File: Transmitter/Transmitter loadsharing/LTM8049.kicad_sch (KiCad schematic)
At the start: 9 parts, among them U12 LTM8049IY-PBF

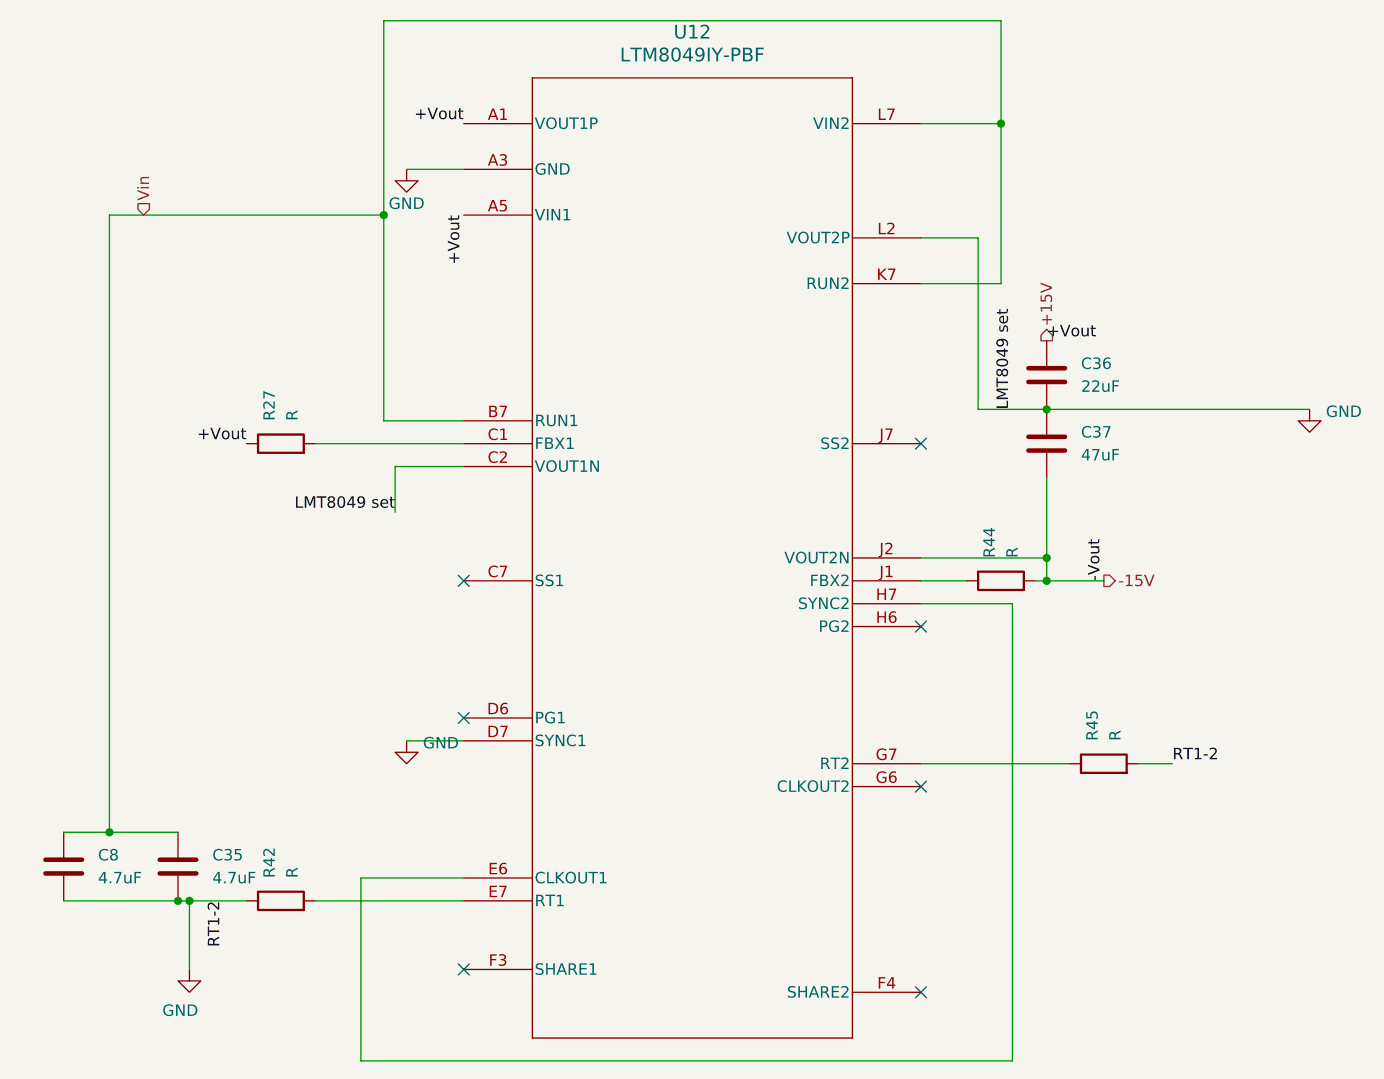
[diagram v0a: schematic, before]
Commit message: routed swithcing regulator
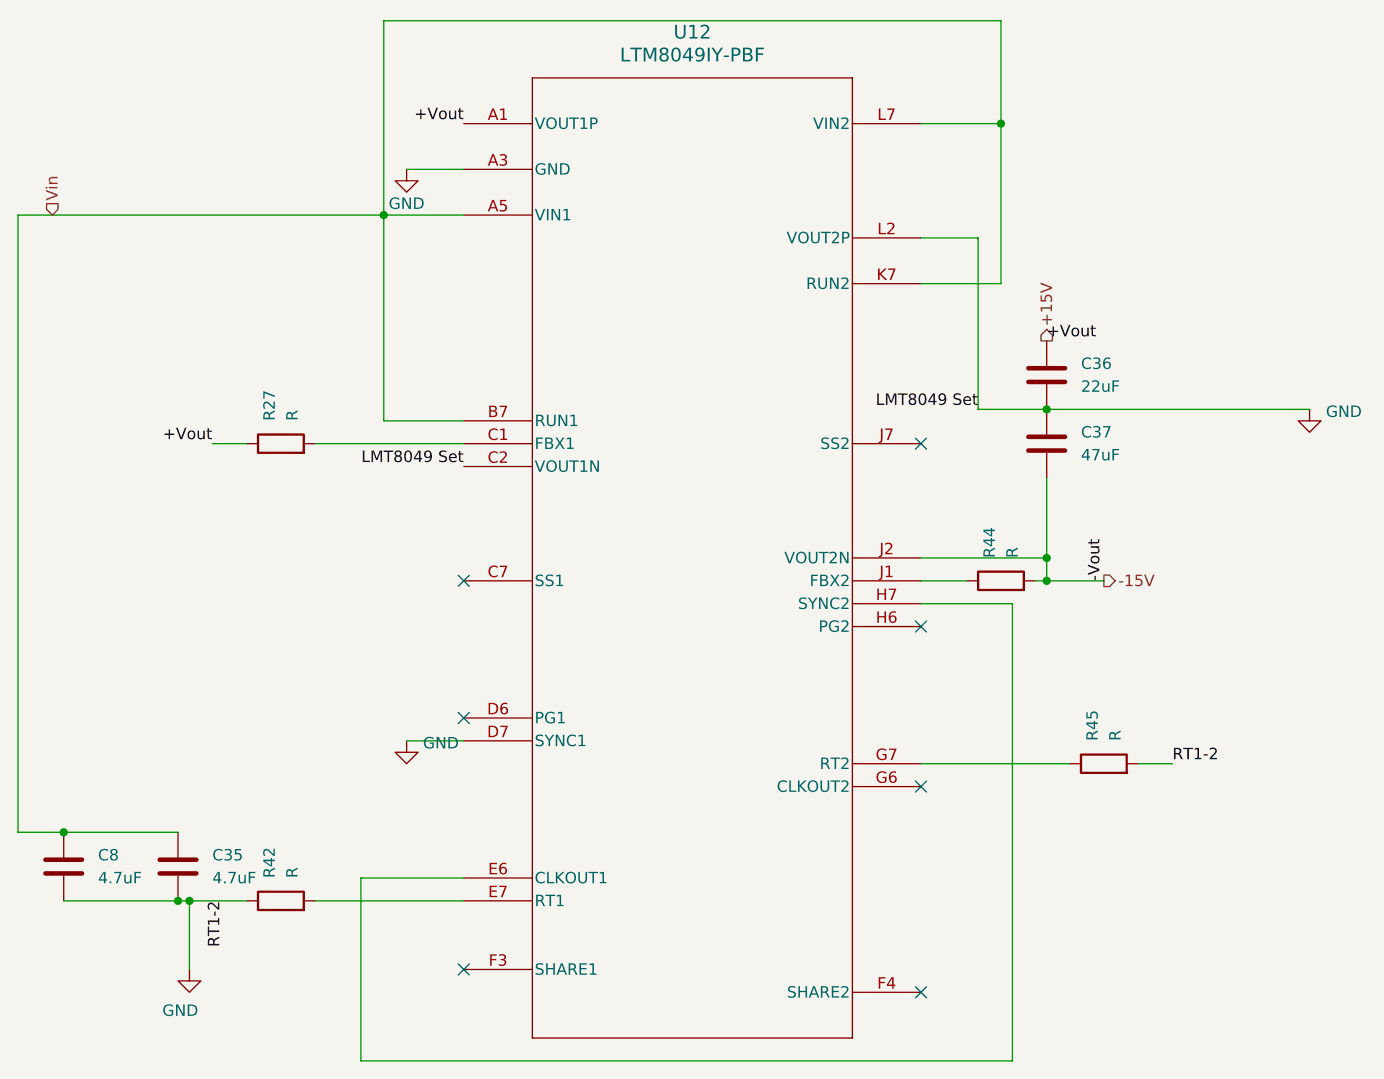
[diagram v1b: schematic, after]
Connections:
- net +15V: no longer U12.A5 (VIN1), U12.A6 (VIN1), U12.A7 (VIN1)
- net Vin: now also U12.A5 (VIN1), U12.A6 (VIN1), U12.A7 (VIN1)
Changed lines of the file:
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@@
+	)
+	(junction
+		(at 63.5 142.24)
+		(diameter 0)
+		(color 0 0 0 0)
 	)
 	(junction
@@
 	)
 	(junction
-		(at 68.58 142.24)
-		(diameter 0)
-		(color 0 0 0 0)
-	)
-	(junction
 		(at 172.72 111.76)
 		(diameter 0)
@@
 	(wire
 		(pts
+			(xy 99.06 73.66) (xy 107.95 73.66)
+		)
+		(stroke
+			(width 0)
+			(type default)
+		)
+	)
+	(wire
+		(pts
 			(xy 172.72 102.87) (xy 172.72 111.76)
 		)
@@
 	(wire
 		(pts
+			(xy 63.5 142.24) (xy 76.2 142.24)
+		)
+		(stroke
+			(width 0)
+			(type default)
+		)
+	)
+	(wire
+		(pts
 			(xy 107.95 96.52) (xy 99.06 96.52)
 		)
@@
 	(wire
 		(pts
-			(xy 100.33 101.6) (xy 107.95 101.6)
-		)
-		(stroke
-			(width 0)
-			(type default)
-		)
-	)
-	(wire
-		(pts
-			(xy 63.5 142.24) (xy 68.58 142.24)
+			(xy 99.06 96.52) (xy 99.06 73.66)
+		)
+		(stroke
+			(width 0)
+			(type default)
+		)
+	)
+	(wire
+		(pts
+			(xy 167.64 81.28) (xy 158.75 81.28)
+		)
+		(stroke
+			(width 0)
+			(type default)
+		)
+	)
+	(wire
+		(pts
+			(xy 58.42 142.24) (xy 58.42 73.66)
+		)
+		(stroke
+			(width 0)
+			(type default)
+		)
+	)
+	(wire
+		(pts
+			(xy 158.75 111.76) (xy 172.72 111.76)
+		)
+		(stroke
+			(width 0)
+			(type default)
+		)
+	)
+	(wire
+		(pts
+			(xy 172.72 95.25) (xy 201.93 95.25)
+		)
+		(stroke
+			(width 0)
+			(type default)
+		)
+	)
+	(wire
+		(pts
+			(xy 167.64 52.07) (xy 167.64 63.5)
+		)
+		(stroke
+			(width 0)
+			(type default)
+		)
+	)
+	(wire
+		(pts
+			(xy 172.72 114.3) (xy 179.07 114.3)
+		)
+		(stroke
+			(width 0)
+			(type default)
+		)
+	)
+	(wire
+		(pts
+			(xy 63.5 149.86) (xy 76.2 149.86)
+		)
+		(stroke
+			(width 0)
+			(type default)
+		)
+	)
+	(wire
+		(pts
+			(xy 58.42 73.66) (xy 99.06 73.66)
+		)
+		(stroke
+			(width 0)
+			(type default)
+		)
+	)
+	(wire
+		(pts
+			(xy 168.91 116.84) (xy 158.75 116.84)
+		)
+		(stroke
+			(width 0)
+			(type default)
+		)
+	)
+	(wire
+		(pts
+			(xy 101.6 132.08) (xy 107.95 132.08)
+		)
+		(stroke
+			(width 0)
+			(type default)
+		)
+	)
+	(wire
+		(pts
+			(xy 167.64 63.5) (xy 167.64 81.28)
 		)
 		(stroke
@@
 	(wire
 		(pts
-			(xy 167.64 81.28) (xy 158.75 81.28)
-		)
-		(stroke
-			(width 0)
-			(type default)
-		)
-	)
-	(wire
-		(pts
-			(xy 68.58 142.24) (xy 68.58 73.66)
-		)
-		(stroke
-			(width 0)
-			(type default)
-		)
-	)
-	(wire
-		(pts
-			(xy 99.06 73.66) (xy 99.06 96.52)
-		)
-		(stroke
-			(width 0)
-			(type default)
-		)
-	)
-	(wire
-		(pts
-			(xy 158.75 111.76) (xy 172.72 111.76)
-		)
-		(stroke
-			(width 0)
-			(type default)
-		)
-	)
-	(wire
-		(pts
-			(xy 172.72 95.25) (xy 201.93 95.25)
-		)
-		(stroke
-			(width 0)
-			(type default)
-		)
-	)
-	(wire
-		(pts
-			(xy 167.64 52.07) (xy 167.64 63.5)
-		)
-		(stroke
-			(width 0)
-			(type default)
-		)
-	)
-	(wire
-		(pts
-			(xy 172.72 114.3) (xy 179.07 114.3)
-		)
-		(stroke
-			(width 0)
-			(type default)
-		)
-	)
-	(wire
-		(pts
-			(xy 63.5 149.86) (xy 76.2 149.86)
-		)
-		(stroke
-			(width 0)
-			(type default)
-		)
-	)
-	(wire
-		(pts
-			(xy 68.58 73.66) (xy 99.06 73.66)
-		)
-		(stroke
-			(width 0)
-			(type default)
-		)
-	)
-	(wire
-		(pts
-			(xy 168.91 116.84) (xy 158.75 116.84)
-		)
-		(stroke
-			(width 0)
-			(type default)
-		)
-	)
-	(wire
-		(pts
-			(xy 101.6 132.08) (xy 107.95 132.08)
-		)
-		(stroke
-			(width 0)
-			(type default)
-		)
-	)
-	(wire
-		(pts
-			(xy 167.64 63.5) (xy 167.64 81.28)
-		)
-		(stroke
-			(width 0)
-			(type default)
-		)
-	)
-	(wire
-		(pts
-			(xy 100.33 106.68) (xy 100.33 101.6)
-		)
-		(stroke
-			(width 0)
-			(type default)
-		)
-	)
-	(wire
-		(pts
 			(xy 107.95 147.32) (xy 96.52 147.32)
 		)
@@
 	(wire
 		(pts
+			(xy 80.01 99.06) (xy 83.82 99.06)
+		)
+		(stroke
+			(width 0)
+			(type default)
+		)
+	)
+	(wire
+		(pts
 			(xy 99.06 52.07) (xy 167.64 52.07)
 		)
@@
 	(wire
 		(pts
-			(xy 68.58 142.24) (xy 76.2 142.24)
+			(xy 58.42 142.24) (xy 63.5 142.24)
 		)
 		(stroke
@@
 		)
 	)
-	(label "+Vout"
-		(at 83.82 99.06 180)
+	(label "LMT8049 Set"
+		(at 165.1 95.25 180)
 		(fields_autoplaced yes)
 		(effects
@@
 		)
 	)
-	(label "LMT8049 set"
-		(at 168.91 95.25 90)
-		(fields_autoplaced yes)
-		(effects
-			(font
-				(size 1.27 1.27)
-			)
-			(justify left bottom)
+	(label "LMT8049 Set"
+		(at 107.95 101.6 180)
+		(fields_autoplaced yes)
+		(effects
+			(font
+				(size 1.27 1.27)
+			)
+			(justify right bottom)
 		)
 	)
@@
 		)
 	)
+	(label "+Vout"
+		(at 80.01 99.06 180)
+		(fields_autoplaced yes)
+		(effects
+			(font
+				(size 1.27 1.27)
+			)
+			(justify right bottom)
+		)
+	)
 	(label "RT1-2"
 		(at 186.69 134.62 0)
@@
 	)
 	(label "+Vout"
-		(at 107.95 73.66 270)
-		(fields_autoplaced yes)
-		(effects
-			(font
-				(size 1.27 1.27)
-			)
-			(justify right bottom)
-		)
-	)
-	(label "LMT8049 set"
-		(at 100.33 106.68 180)
-		(fields_autoplaced yes)
-		(effects
-			(font
-				(size 1.27 1.27)
-			)
-			(justify right bottom)
-		)
-	)
-	(label "+Vout"
 		(at 107.95 63.5 180)
 		(fields_autoplaced yes)
@@
 	(hierarchical_label "Vin"
 		(shape input)
-		(at 72.39 73.66 90)
-		(fields_autoplaced yes)
-		(effects
+		(at 62.23 73.66 90)
+		(fields_autoplaced yes)
+		(effects
